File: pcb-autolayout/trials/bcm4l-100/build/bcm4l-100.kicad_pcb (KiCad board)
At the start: 4 copper layers, 80 x 60 mm, 120 parts, among them J1 MicroFit 2x4, J2 MicroFit 2x6, J3 SWD, Q1 SQD40P06 (P-MOS), Q11 AO3401A, Q12 MMBT3904, Q13 AO3401A, Q14 MMBT3904, Q15 AO3401A, Q16 MMBT3904, Q17 AO3401A, Q18 MMBT3904, SW1 RESET, U1 TPS54202, U2 AMS1117-3.3, U3 TJA1051T/3, U4 TJA1021T/20, U5 STM32F103C8T6, Y1 8MHz

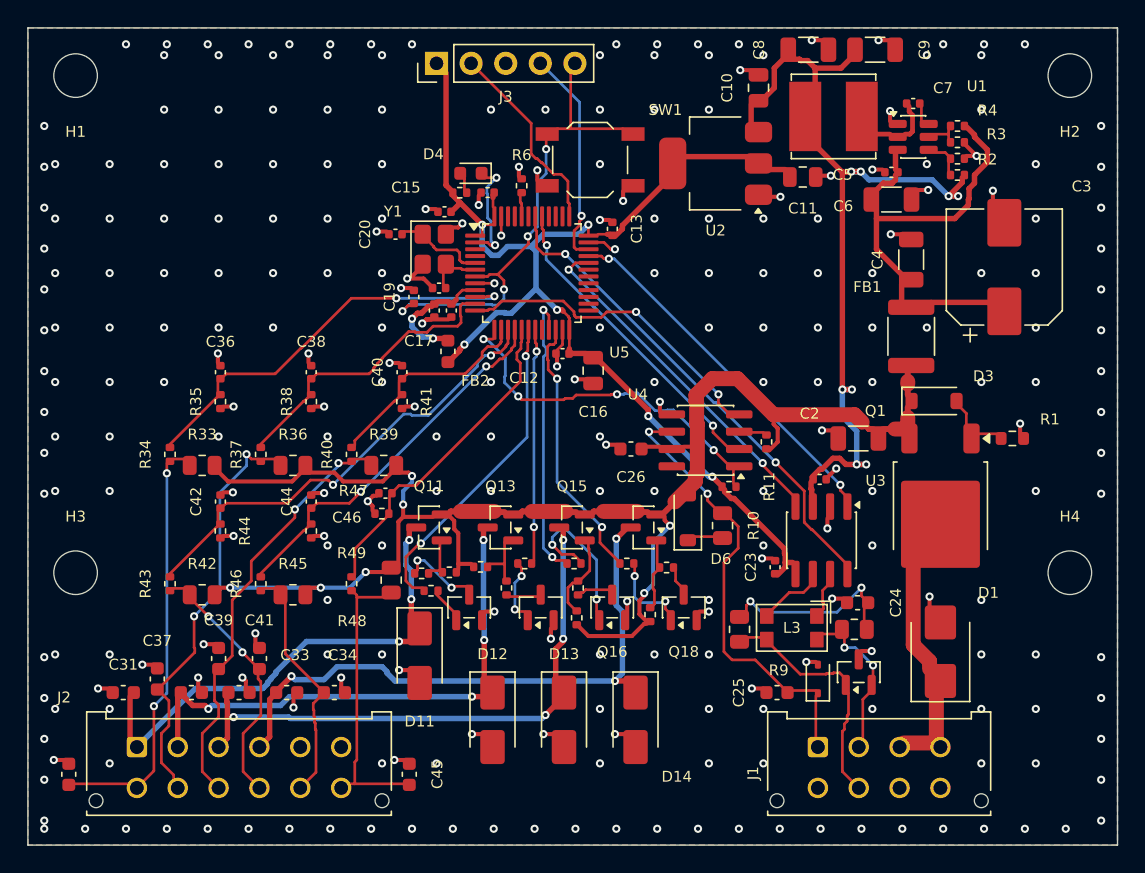
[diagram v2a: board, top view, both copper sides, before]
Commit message: bench R sau sửa review: bcm4l 16/16; synth-hi hết chập (DRC 21 -> 0) đổi 2 chân hở; synth-lo TỤT 0 -> 1 hở (đang truy)
bench ghi build/run.log từng trial để truy hồi quy.

Co-Authored-By: Claude Opus 5.5 <noreply@anthropic.com>
Claude-Session: https://claude.ai/code/session_012jwodCpQFB8wopi3P3TnUz
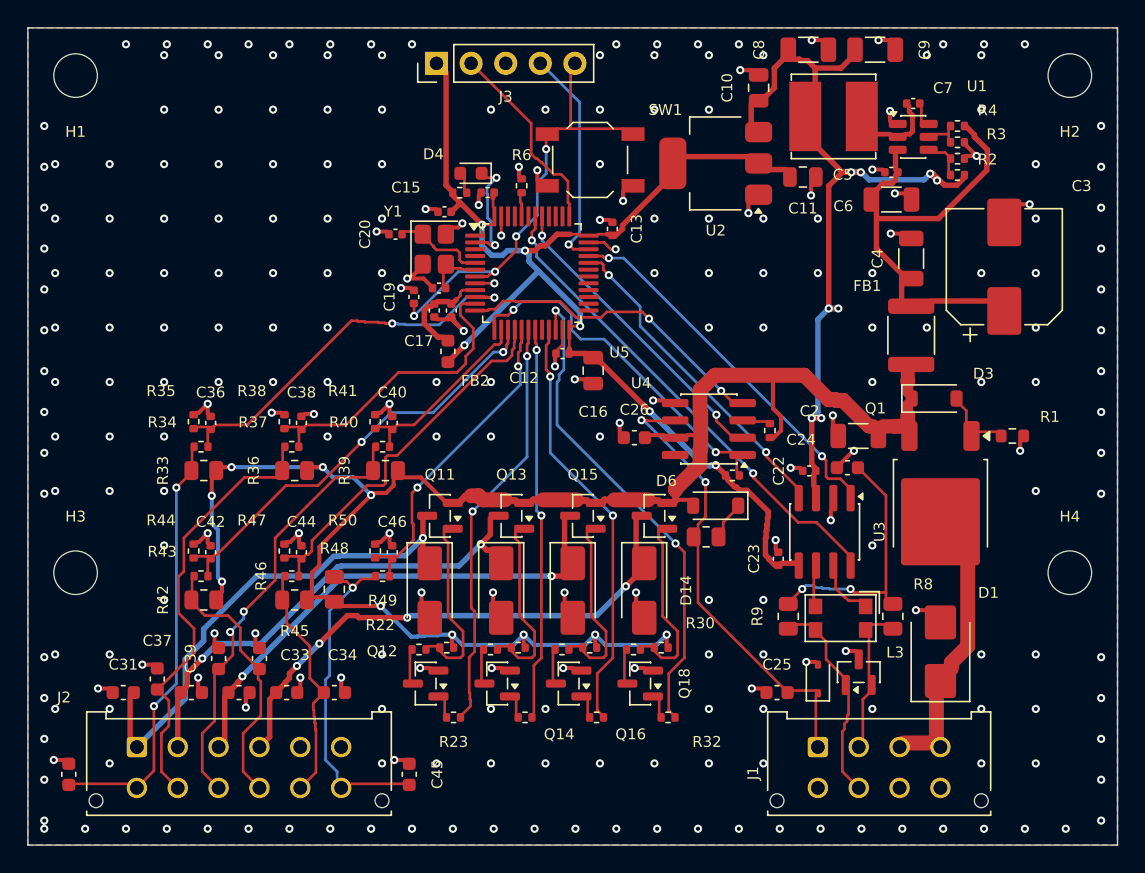
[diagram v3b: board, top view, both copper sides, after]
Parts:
- C20: renamed from C40; value 10n -> 20p
- C46: renamed from C20; value 20p -> 10n
- Q11: renamed from Q12; value MMBT3904 -> AO3401A
- Q12: renamed from Q11; value AO3401A -> MMBT3904
- Q13: renamed from Q14; value MMBT3904 -> AO3401A
- Q14: renamed from Q13; value AO3401A -> MMBT3904
- Q15: renamed from Q16; value MMBT3904 -> AO3401A
- Q16: renamed from Q15; value AO3401A -> MMBT3904
- Q17: renamed from Q18; value MMBT3904 -> AO3401A
- Q18: renamed from Q17; value AO3401A -> MMBT3904
- R21: renamed from R23; value 1k -> 10k
- R23: renamed from R21; value 10k -> 1k
- R28: renamed from R29; value 1k -> 10k
- R29: renamed from R28; value 10k -> 1k
- R31: renamed from R32; value 1k -> 10k
- R32: renamed from R31; value 10k -> 1k
- R34: renamed from R44; value 10k -> 47k
- R35: renamed from R43; value 47k -> 10k
- R37: renamed from R47; value 10k -> 47k
- R38: renamed from R46; value 47k -> 10k
- R40: renamed from R41; value 10k -> 47k
- R41: renamed from R49; value 47k -> 10k
- R43: renamed from R35; value 10k -> 47k
- R44: renamed from R34; value 47k -> 10k
- R46: renamed from R38; value 10k -> 47k
- R47: renamed from R37; value 47k -> 10k
- R49: renamed from R50; value 10k -> 47k
- R50: renamed from R40; value 47k -> 10k
- moved C46 23.4 mm to (126.8, 98.5), turned to 90 degrees
- moved R43 12.9 mm to (112.7, 100.2), turned to 0 degrees
- moved R46 12.9 mm to (119.4, 100.2), turned to 0 degrees
- moved R35 12.0 mm to (112.2, 88.9)
- moved R41 12.0 mm to (125.5, 88.9)
- moved R38 12.0 mm to (118.8, 88.9)
- moved Q12 11.5 mm to (129.2, 108.1)
- moved Q14 11.5 mm to (134.5, 108.1)
- moved Q16 11.5 mm to (139.7, 108.1)
- moved Q18 11.5 mm to (145.0, 108.1)
- moved R26 11.3 mm to (136.5, 110.6)
- moved R32 11.0 mm to (147.0, 110.6), turned to 180 degrees
- moved R23 10.7 mm to (131.2, 110.6)
- moved C20 10.1 mm to (127.0, 75.2), turned to 180 degrees
- moved C24 9.94 mm to (160.2, 92.3)
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- renumbered C46 to C40, R25 to R24, R24 to R25, R48 to R39, R39 to R48
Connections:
- C20 pad 1: IN3_M -> OSC_IN
- C40 pad 1: IN6_M -> IN3_M
- C46 pad 1: OSC_IN -> IN6_M
- Q11 pad 1: OUT1_B -> OUT1_G
- Q11 pad 2: GND -> VBAT_P
- Q11 pad 3: OUT1_C -> OUT1
- Q12 pad 1: OUT1_G -> OUT1_B
- Q12 pad 2: VBAT_P -> GND
- Q12 pad 3: OUT1 -> OUT1_C
- Q13 pad 1: OUT2_B -> OUT2_G
- Q13 pad 2: GND -> VBAT_P
- Q13 pad 3: OUT2_C -> OUT2
- Q14 pad 1: OUT2_G -> OUT2_B
- Q14 pad 2: VBAT_P -> GND
- Q14 pad 3: OUT2 -> OUT2_C
- Q15 pad 1: OUT3_B -> OUT3_G
- Q15 pad 2: GND -> VBAT_P
- Q15 pad 3: OUT3_C -> OUT3
- Q16 pad 1: OUT3_G -> OUT3_B
- Q16 pad 2: VBAT_P -> GND
- Q16 pad 3: OUT3 -> OUT3_C
- Q17 pad 1: OUT4_B -> OUT4_G
- Q17 pad 2: GND -> VBAT_P
- Q17 pad 3: OUT4_C -> OUT4
- Q18 pad 1: OUT4_G -> OUT4_B
- Q18 pad 2: VBAT_P -> GND
- Q18 pad 3: OUT4 -> OUT4_C
- R21 pad 1: OUT1_M -> VBAT_P
- R21 pad 2: OUT1_B -> OUT1_G
- R23 pad 1: VBAT_P -> OUT1_M
- R23 pad 2: OUT1_G -> OUT1_B
- R24 pad 1: OUT2_G -> VBAT_P
- R24 pad 2: OUT2_C -> OUT2_G
- R25 pad 1: VBAT_P -> OUT2_G
- R25 pad 2: OUT2_G -> OUT2_C
- R28 pad 1: OUT3_M -> OUT3_G
- R28 pad 2: OUT3_B -> OUT3_C
- R29 pad 1: OUT3_G -> OUT3_M
- R29 pad 2: OUT3_C -> OUT3_B
- R31 pad 1: OUT4_M -> OUT4_G
- R31 pad 2: OUT4_B -> OUT4_C
- R32 pad 1: OUT4_G -> OUT4_M
- R32 pad 2: OUT4_C -> OUT4_B
- R34 pad 1: IN4_M -> IN1
- R34 pad 2: GND -> IN1_M
- R35 pad 1: IN4 -> IN1_M
- R35 pad 2: IN4_M -> GND
- R37 pad 1: IN5_M -> IN2
- R37 pad 2: GND -> IN2_M
- R38 pad 1: IN5 -> IN2_M
- R38 pad 2: IN5_M -> GND
- R39 pad 2: IN6 -> IN3
- R40 pad 1: IN3_M -> IN3
- R40 pad 2: GND -> IN3_M
- R41 pad 1: IN6 -> IN3_M
- R41 pad 2: IN6_M -> GND
- R43 pad 1: IN1_M -> IN4
- R43 pad 2: GND -> IN4_M
- R44 pad 1: IN1 -> IN4_M
- R44 pad 2: IN1_M -> GND
- R46 pad 1: IN2_M -> IN5
- R46 pad 2: GND -> IN5_M
- R47 pad 1: IN2 -> IN5_M
- R47 pad 2: IN2_M -> GND
- R48 pad 2: IN3 -> IN6
- R49 pad 1: IN6_M -> IN6
- R49 pad 2: GND -> IN6_M
- R50 pad 1: IN3 -> IN6_M
- R50 pad 2: IN3_M -> GND
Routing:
- net OUT4_M: track 18.9 -> 35.3 mm
- net VBAT_P: track 102.6 -> 116.6 mm, vias 7 -> 10
- net OUT2_M: track 16.4 -> 28.0 mm
- net OUT3_B: track 11.2 -> 1.15 mm, vias 2 -> 0
- net OUT1_G: track 2.60 -> 12.4 mm
- net OUT3_M: track 20.6 -> 30.3 mm
- net OUT2_G: track 3.75 -> 12.4 mm
- net OUT4_G: track 4.36 -> 12.4 mm
- net OUT3_G: track 5.44 -> 12.4 mm
- net OUT1_M: track 23.0 -> 29.8 mm
- net OUT4: track 42.4 -> 35.9 mm, vias 3 -> 4
- net OUT3: track 39.3 -> 33.7 mm, vias 4 -> 2
- net CAN_SPL: track 12.2 -> 17.6 mm
- net OUT4_B: track 5.54 -> 1.15 mm, vias 2 -> 0
- net OUT2: track 37.2 -> 33.4 mm, vias 4 -> 2
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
